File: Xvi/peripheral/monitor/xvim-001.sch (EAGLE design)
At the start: 7 parts

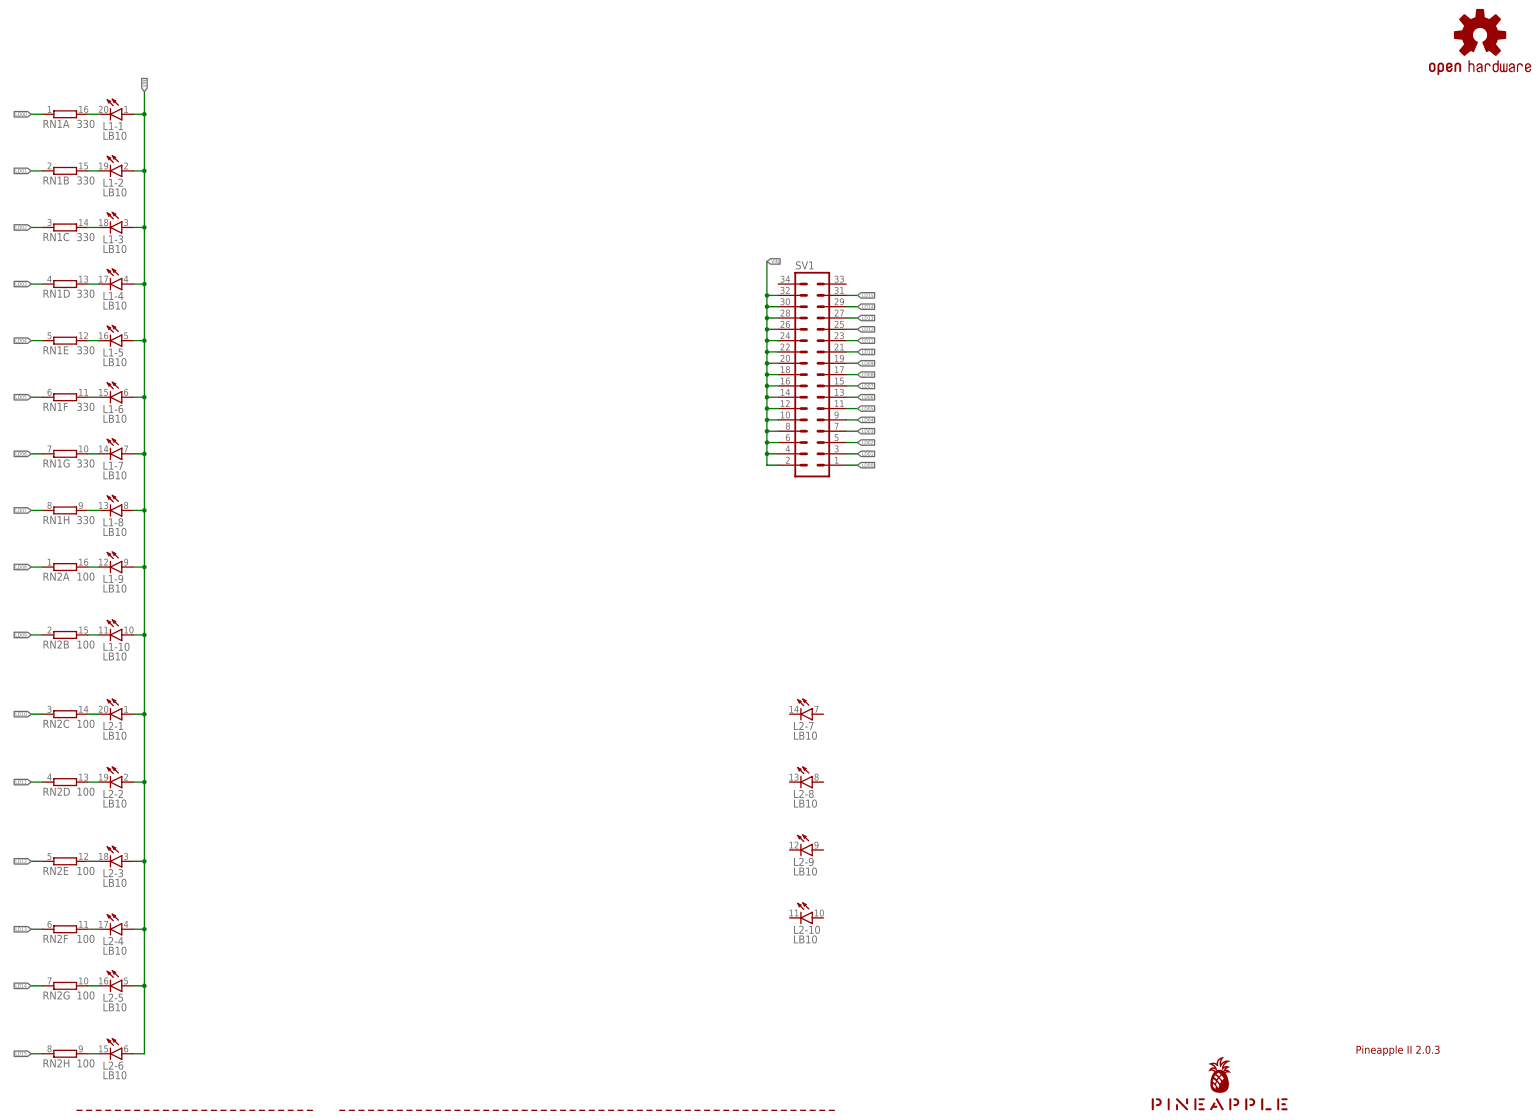
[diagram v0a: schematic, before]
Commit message: Fixed monitor board.
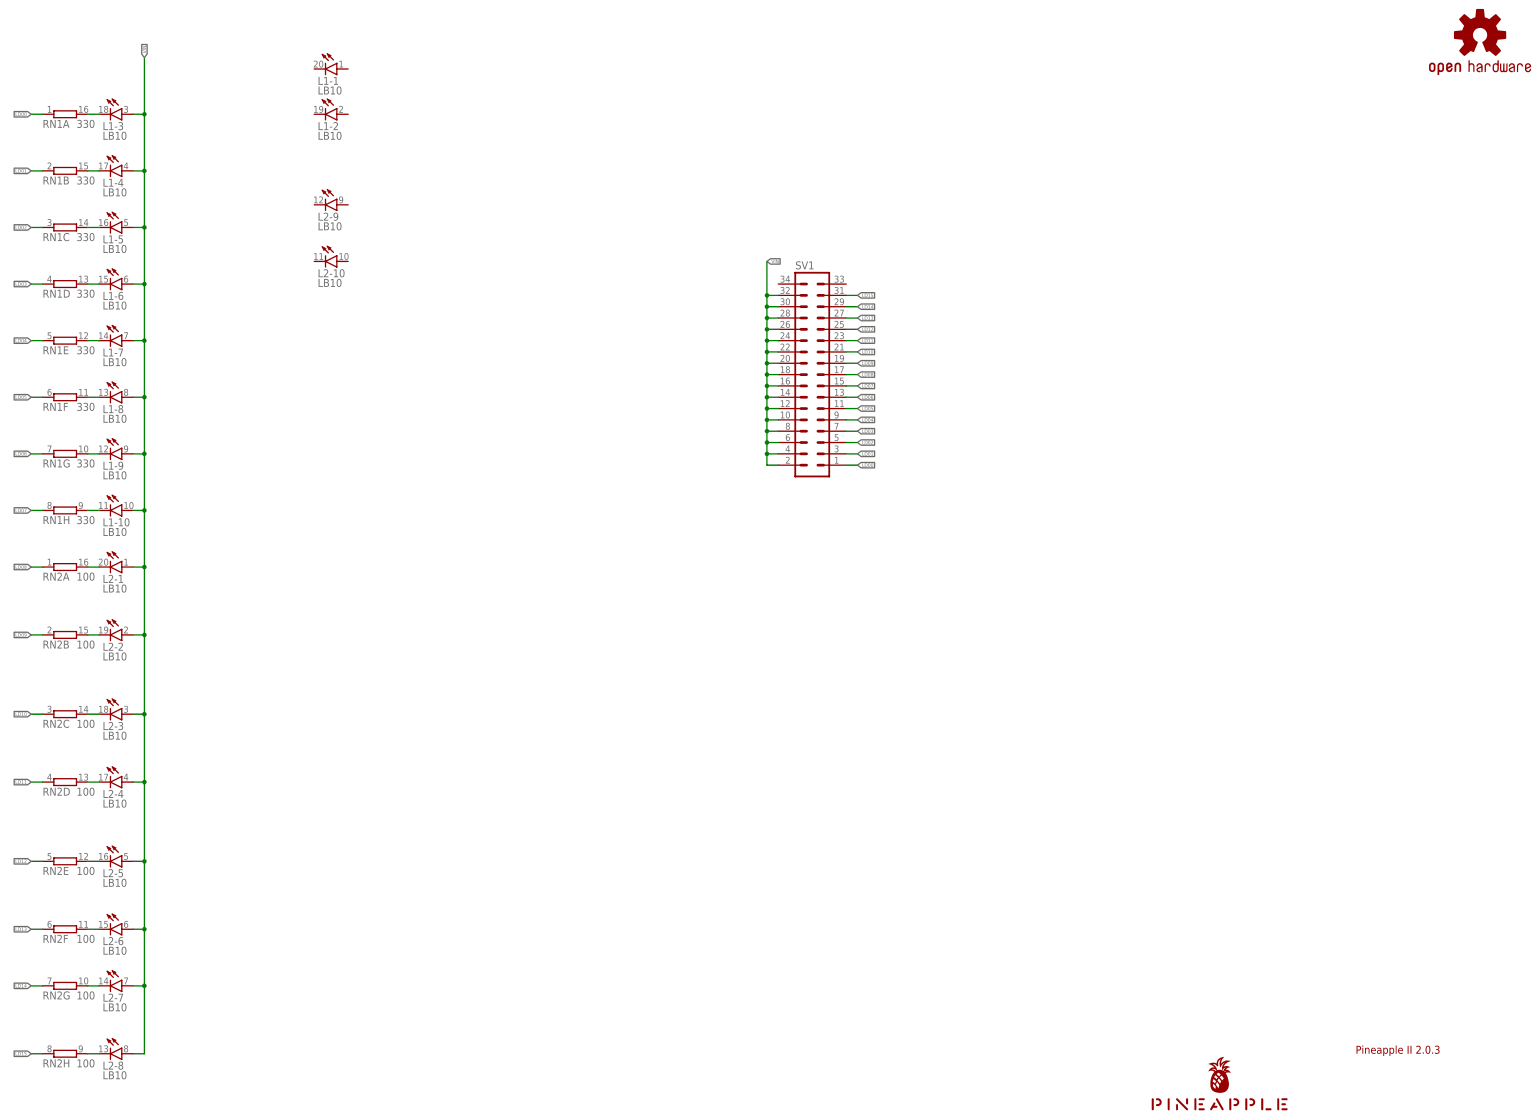
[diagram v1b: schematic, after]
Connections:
- removed net LED1K: L1-1.C, RN1A.2
- removed net LED2K: L1-2.C, RN1B.2
- removed net LED3K: L1-3.C, RN1C.2
- removed net LED4K: L1-4.C, RN1D.2
- removed net LED5K: L1-5.C, RN1E.2
- removed net LED6K: L1-6.C, RN1F.2
- new net N$11: L1-9.C, RN1G.2
- new net N$12: L1-7.C, RN1E.2
- new net N$13: L1-6.C, RN1D.2
- new net N$14: L1-5.C, RN1C.2
- new net N$15: L1-4.C, RN1B.2
- new net N$16: L1-3.C, RN1A.2
- net N$1: now also L2-8.C, RN2H.2; no longer L1-7.C, RN1G.2
- net N$10: now also L1-8.C, RN1F.2; no longer L2-6.C, RN2H.2
- net N$2: now also L2-7.C, RN2G.2; no longer L1-8.C, RN1H.2
- net N$3: now also L2-6.C, RN2F.2; no longer L1-9.C, RN2A.2
- net N$4: now also L2-5.C, RN2E.2; no longer L1-10.C, RN2B.2
- net N$5: now also L2-4.C, RN2D.2; no longer L2-1.C, RN2C.2
- net N$6: now also L2-3.C, RN2C.2; no longer L2-2.C, RN2D.2
- net N$7: now also L2-2.C, RN2B.2; no longer L2-3.C, RN2E.2
- net N$8: now also L2-1.C, RN2A.2; no longer L2-4.C, RN2F.2
- net N$9: now also L1-10.C, RN1H.2; no longer L2-5.C, RN2G.2
- net VIN: now also L2-7.A, L2-8.A; no longer L1-1.A, L1-2.A
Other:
- moved on the sheet: L1-1, L1-10, L1-2, L1-3, L1-4, L1-5, L1-6, L1-7, L1-8, L1-9, L2-1, L2-10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

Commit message: Fixed positions of the components.
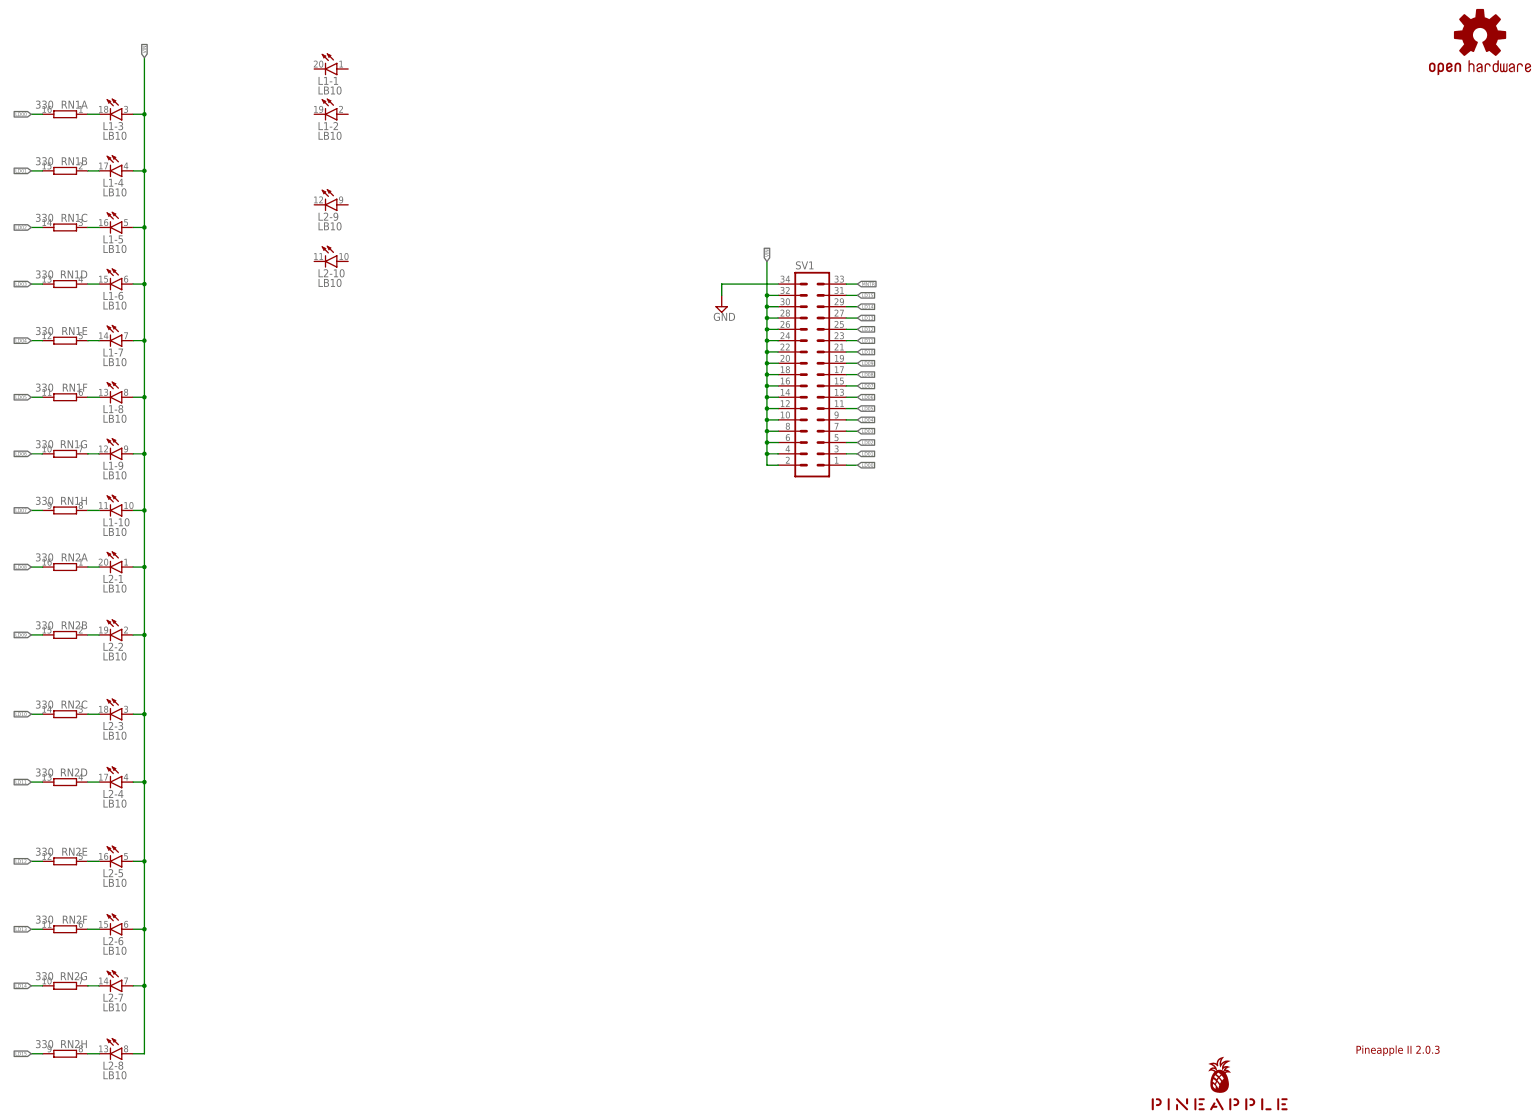
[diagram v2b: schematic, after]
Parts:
- RN2: value 100 -> 330
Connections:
- new net GND: SV1.34
- new net MNTR: SV1.33
- net LD00: now also RN1A.2; no longer RN1A.1
- net LD01: now also RN1B.2; no longer RN1B.1
- net LD02: now also RN1C.2; no longer RN1C.1
- net LD03: now also RN1D.2; no longer RN1D.1
- net LD04: now also RN1E.2; no longer RN1E.1
- net LD05: now also RN1F.2; no longer RN1F.1
- net LD06: now also RN1G.2; no longer RN1G.1
- net LD07: now also RN1H.2; no longer RN1H.1
- net LD08: now also RN2A.2; no longer RN2A.1
- net LD09: now also RN2B.2; no longer RN2B.1
- net LD10: now also RN2C.2; no longer RN2C.1
- net LD11: now also RN2D.2; no longer RN2D.1
- net LD12: now also RN2E.2; no longer RN2E.1
- net LD13: now also RN2F.2; no longer RN2F.1
- net LD14: now also RN2G.2; no longer RN2G.1
- net LD15: now also RN2H.2; no longer RN2H.1
- net N$1: now also L1-3.C, RN1A.1; no longer L2-8.C, RN2H.2
- net N$10: now also L2-2.C, RN2B.1; no longer L1-8.C, RN1F.2
- net N$11: now also L2-3.C, RN2C.1; no longer L1-9.C, RN1G.2
- net N$12: now also L2-4.C, RN2D.1; no longer L1-7.C, RN1E.2
- net N$13: now also L2-5.C, RN2E.1; no longer L1-6.C, RN1D.2
- net N$14: now also L2-6.C, RN2F.1; no longer L1-5.C, RN1C.2
- net N$15: now also L2-7.C, RN2G.1; no longer L1-4.C, RN1B.2
- net N$16: now also L2-8.C, RN2H.1; no longer L1-3.C, RN1A.2
- net N$2: now also L1-4.C, RN1B.1; no longer L2-7.C, RN2G.2
- net N$3: now also L1-5.C, RN1C.1; no longer L2-6.C, RN2F.2
- net N$4: now also L1-6.C, RN1D.1; no longer L2-5.C, RN2E.2
- net N$5: now also L1-7.C, RN1E.1; no longer L2-4.C, RN2D.2
- net N$6: now also L1-8.C, RN1F.1; no longer L2-3.C, RN2C.2
- net N$7: now also L1-9.C, RN1G.1; no longer L2-2.C, RN2B.2
- net N$8: now also L1-10.C, RN1H.1; no longer L2-1.C, RN2A.2
- net N$9: now also L2-1.C, RN2A.1; no longer L1-10.C, RN1H.2
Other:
- moved on the sheet: RN1A, RN1B, RN1C, RN1D, RN1E, RN1F, RN1G, RN1H, RN2A, RN2B, RN2C, RN2D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
